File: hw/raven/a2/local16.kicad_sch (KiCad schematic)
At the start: 34 parts, among them J401 IDE44, J403 BatteryHolder, U401 MC68901, U402 ATF22V10C-10PU, U403 MC68901, U404 MAX3245CAI+T, U405 YM2149, U406 DS1307, U407 24AA02E48, X401 8Mhz (5V)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

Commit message: a2, reannotate
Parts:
- renumbered J403 to J402, R344 to R408
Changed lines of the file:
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@@
 		(on_board yes)
 		(dnp no)
-		(property "Reference" "#PWR0436"
+		(property "Reference" "#PWR0434"
 			(at 271.145 208.28 0)
 			(effects
@@
 			(project "raven"
 				(path "/af55e73e-5814-45b4-ac5c-0bab62c0b1c7/dacbbff1-3783-4e73-aa71-dbe41700eceb"
-					(reference "#PWR0436")
+					(reference "#PWR0434")
 					(unit 1)
 				)
@@
 		(on_board yes)
 		(dnp no)
-		(property "Reference" "J403"
+		(property "Reference" "J402"
 			(at 205.105 208.28 0)
 			(effects
@@
 			(project "raven"
 				(path "/af55e73e-5814-45b4-ac5c-0bab62c0b1c7/dacbbff1-3783-4e73-aa71-dbe41700eceb"
-					(reference "J403")
+					(reference "J402")
 					(unit 1)
 				)
@@
 		(on_board yes)
 		(dnp no)
-		(property "Reference" "#PWR0432"
+		(property "Reference" "#PWR0430"
 			(at 201.295 201.93 0)
 			(effects
@@
 			(project "raven"
 				(path "/af55e73e-5814-45b4-ac5c-0bab62c0b1c7/dacbbff1-3783-4e73-aa71-dbe41700eceb"
-					(reference "#PWR0432")
+					(reference "#PWR0430")
 					(unit 1)
 				)
@@
 		(on_board yes)
 		(dnp no)
-		(property "Reference" "#PWR0444"
+		(property "Reference" "#PWR0443"
 			(at 85.09 242.57 0)
 			(effects
@@
 			(project "raven"
 				(path "/af55e73e-5814-45b4-ac5c-0bab62c0b1c7/dacbbff1-3783-4e73-aa71-dbe41700eceb"
-					(reference "#PWR0444")
+					(reference "#PWR0443")
 					(unit 1)
 				)
@@
 		(on_board yes)
 		(dnp no)
-		(property "Reference" "#PWR0447"
+		(property "Reference" "#PWR0446"
 			(at 171.45 300.99 0)
 			(effects
@@
 			(project "raven"
 				(path "/af55e73e-5814-45b4-ac5c-0bab62c0b1c7/dacbbff1-3783-4e73-aa71-dbe41700eceb"
-					(reference "#PWR0447")
+					(reference "#PWR0446")
 					(unit 1)
 				)
@@
 		(on_board yes)
 		(dnp no)
-		(property "Reference" "#PWR0433"
+		(property "Reference" "#PWR0431"
 			(at 271.145 198.12 0)
 			(effects
@@
 			(project "raven"
 				(path "/af55e73e-5814-45b4-ac5c-0bab62c0b1c7/dacbbff1-3783-4e73-aa71-dbe41700eceb"
-					(reference "#PWR0433")
+					(reference "#PWR0431")
 					(unit 1)
 				)
@@
 		(on_board yes)
 		(dnp no)
-		(property "Reference" "#PWR0443"
+		(property "Reference" "#PWR0442"
 			(at 57.785 242.57 0)
 			(effects
@@
 			(project "raven"
 				(path "/af55e73e-5814-45b4-ac5c-0bab62c0b1c7/dacbbff1-3783-4e73-aa71-dbe41700eceb"
-					(reference "#PWR0443")
+					(reference "#PWR0442")
 					(unit 1)
 				)
@@
 		(on_board yes)
 		(dnp no)
-		(property "Reference" "#PWR0439"
+		(property "Reference" "#PWR0438"
 			(at 178.435 228.6 0)
 			(effects
@@
 			(project "raven"
 				(path "/af55e73e-5814-45b4-ac5c-0bab62c0b1c7/dacbbff1-3783-4e73-aa71-dbe41700eceb"
-					(reference "#PWR0439")
+					(reference "#PWR0438")
 					(unit 1)
 				)
@@
 		(on_board yes)
 		(dnp no)
-		(property "Reference" "#PWR0440"
+		(property "Reference" "#PWR0439"
 			(at 222.885 228.6 0)
 			(effects
@@
 			(project "raven"
 				(path "/af55e73e-5814-45b4-ac5c-0bab62c0b1c7/dacbbff1-3783-4e73-aa71-dbe41700eceb"
-					(reference "#PWR0440")
+					(reference "#PWR0439")
 					(unit 1)
 				)
@@
 		(dnp no)
 		(fields_autoplaced yes)
-		(property "Reference" "#PWR0442"
+		(property "Reference" "#PWR0441"
 			(at 424.18 239.395 0)
 			(effects
@@
 			(project "raven"
 				(path "/af55e73e-5814-45b4-ac5c-0bab62c0b1c7/dacbbff1-3783-4e73-aa71-dbe41700eceb"
-					(reference "#PWR0442")
+					(reference "#PWR0441")
 					(unit 1)
 				)
@@
 		(on_board yes)
 		(dnp no)
-		(property "Reference" "#PWR0446"
+		(property "Reference" "#PWR0445"
 			(at 194.945 278.765 0)
 			(effects
@@
 			(project "raven"
 				(path "/af55e73e-5814-45b4-ac5c-0bab62c0b1c7/dacbbff1-3783-4e73-aa71-dbe41700eceb"
-					(reference "#PWR0446")
+					(reference "#PWR0445")
 					(unit 1)
 				)
@@
 		(on_board yes)
 		(dnp no)
-		(property "Reference" "#PWR0438"
+		(property "Reference" "#PWR0437"
 			(at 398.78 220.98 0)
 			(effects
@@
 			(project "raven"
 				(path "/af55e73e-5814-45b4-ac5c-0bab62c0b1c7/dacbbff1-3783-4e73-aa71-dbe41700eceb"
-					(reference "#PWR0438")
+					(reference "#PWR0437")
 					(unit 1)
 				)
@@
 		(dnp no)
 		(fields_autoplaced yes)
-		(property "Reference" "#PWR0441"
+		(property "Reference" "#PWR0440"
 			(at 288.29 237.49 0)
 			(effects
@@
 			(project "raven"
 				(path "/af55e73e-5814-45b4-ac5c-0bab62c0b1c7/dacbbff1-3783-4e73-aa71-dbe41700eceb"
-					(reference "#PWR0441")
+					(reference "#PWR0440")
 					(unit 1)
 				)
@@
 		(on_board yes)
 		(dnp no)
-		(property "Reference" "#PWR0437"
+		(property "Reference" "#PWR0435"
 			(at 28.575 218.44 0)
 			(effects
@@
 			(project "raven"
 				(path "/af55e73e-5814-45b4-ac5c-0bab62c0b1c7/dacbbff1-3783-4e73-aa71-dbe41700eceb"
-					(reference "#PWR0437")
+					(reference "#PWR0435")
 					(unit 1)
 				)
@@
 		(on_board yes)
 		(dnp no)
-		(property "Reference" "R344"
+		(property "Reference" "R408"
 			(at 344.17 213.36 90)
 			(effects
@@
 			(project "raven"
 				(path "/af55e73e-5814-45b4-ac5c-0bab62c0b1c7/dacbbff1-3783-4e73-aa71-dbe41700eceb"
-					(reference "R344")
+					(reference "R408")
 					(unit 1)
 				)
@@
 		(on_board yes)
 		(dnp no)
-		(property "Reference" "#PWR0638"
+		(property "Reference" "#PWR0436"
 			(at 344.17 220.98 0)
 			(effects
@@
 			(project "raven"
 				(path "/af55e73e-5814-45b4-ac5c-0bab62c0b1c7/dacbbff1-3783-4e73-aa71-dbe41700eceb"
-					(reference "#PWR0638")
+					(reference "#PWR0436")
 					(unit 1)
 				)
@@
 		(on_board yes)
 		(dnp no)
-		(property "Reference" "#PWR0435"
+		(property "Reference" "#PWR0433"
 			(at 40.64 210.185 0)
 			(effects
@@
 			(project "raven"
 				(path "/af55e73e-5814-45b4-ac5c-0bab62c0b1c7/dacbbff1-3783-4e73-aa71-dbe41700eceb"
-					(reference "#PWR0435")
+					(reference "#PWR0433")
 					(unit 1)
 				)
@@
 		(on_board yes)
 		(dnp no)
-		(property "Reference" "#PWR0445"
+		(property "Reference" "#PWR0444"
 			(at 171.45 273.05 0)
 			(effects
@@
 			(project "raven"
 				(path "/af55e73e-5814-45b4-ac5c-0bab62c0b1c7/dacbbff1-3783-4e73-aa71-dbe41700eceb"
-					(reference "#PWR0445")
+					(reference "#PWR0444")
 					(unit 1)
 				)
@@
 		(on_board yes)
 		(dnp no)
-		(property "Reference" "#PWR0434"
+		(property "Reference" "#PWR0432"
 			(at 260.985 200.66 0)
 			(effects
@@
 			(project "raven"
 				(path "/af55e73e-5814-45b4-ac5c-0bab62c0b1c7/dacbbff1-3783-4e73-aa71-dbe41700eceb"
-					(reference "#PWR0434")
+					(reference "#PWR0432")
 					(unit 1)
 				)
@@
 		(on_board yes)
 		(dnp no)
-		(property "Reference" "#PWR0431"
+		(property "Reference" "#PWR0429"
 			(at 178.435 196.85 0)
 			(effects
@@
 			(project "raven"
 				(path "/af55e73e-5814-45b4-ac5c-0bab62c0b1c7/dacbbff1-3783-4e73-aa71-dbe41700eceb"
-					(reference "#PWR0431")
+					(reference "#PWR0429")
 					(unit 1)
 				)

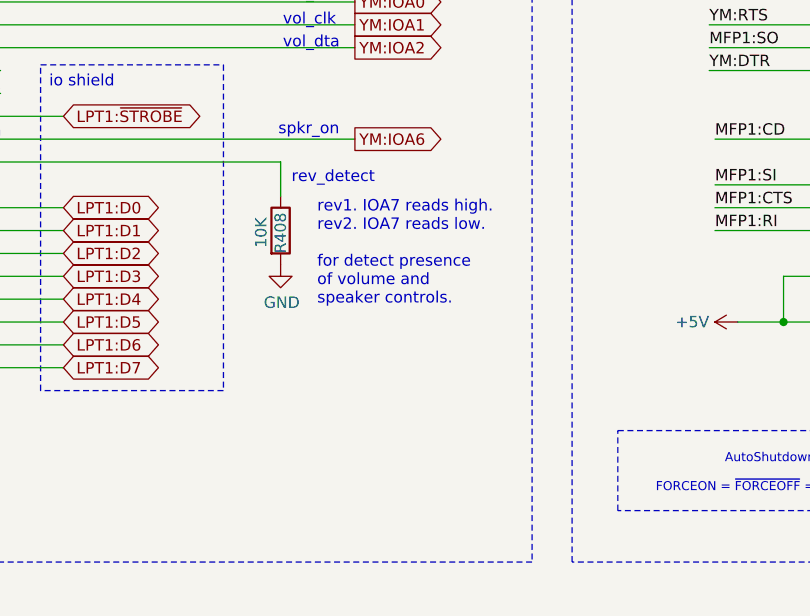
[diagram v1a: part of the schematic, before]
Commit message: A2: dac + adc + dsp work
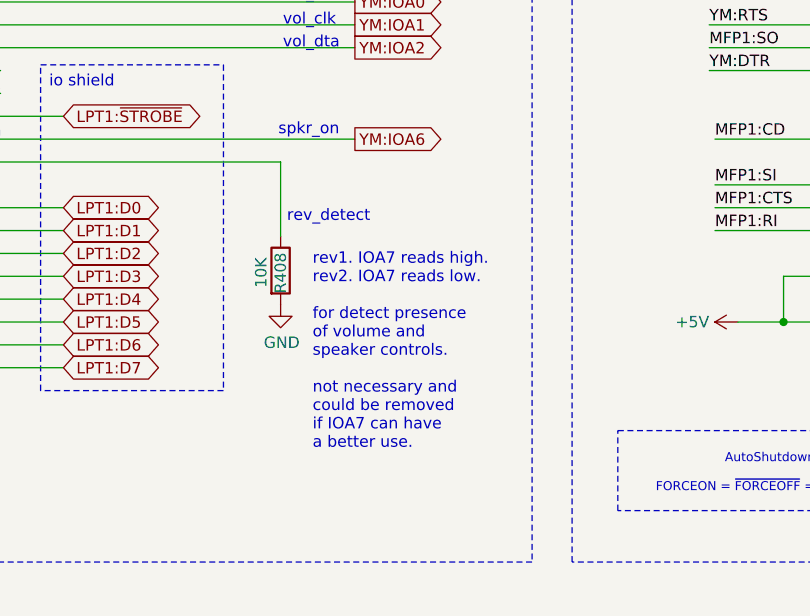
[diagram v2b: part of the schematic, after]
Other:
- note added: "rev1. IOA7 reads high. rev2. IOA7 reads low. for detect presence of volume and speaker controls. not necessary and could be removed if IOA7 can have a better use."
- note removed: "rev1. IOA7 reads high. rev2. IOA7 reads low. for detect presence of volume and speaker controls."
- moved on the sheet: R408

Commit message: misc a2 work
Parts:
- J402: footprint S8401-46 -> 68k:S8401-46
- U406: footprint SOIC127P600X175-8N -> 68k:SOIC127P600X175-8N
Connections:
- net MFP2:TCO renamed ~{IRQ_VBL}
- no-connect marks 22 -> 20
